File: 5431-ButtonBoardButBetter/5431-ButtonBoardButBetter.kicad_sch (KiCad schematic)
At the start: 17 parts, among them SW1 SW_DIP_x01, SW10 SW_DIP_x01, SW11 SW_DIP_x01, SW12 SW_DIP_x01, SW13 SW_DIP_x01, SW14 SW_DIP_x01, SW15 SW_DIP_x01, SW16 SW_DIP_x01, SW2 SW_DIP_x01, SW3 SW_DIP_x01, SW4 SW_DIP_x01, SW5 SW_DIP_x01, SW6 SW_DIP_x01, SW7 SW_DIP_x01, SW8 SW_DIP_x01, SW9 SW_DIP_x01, U1 Pico

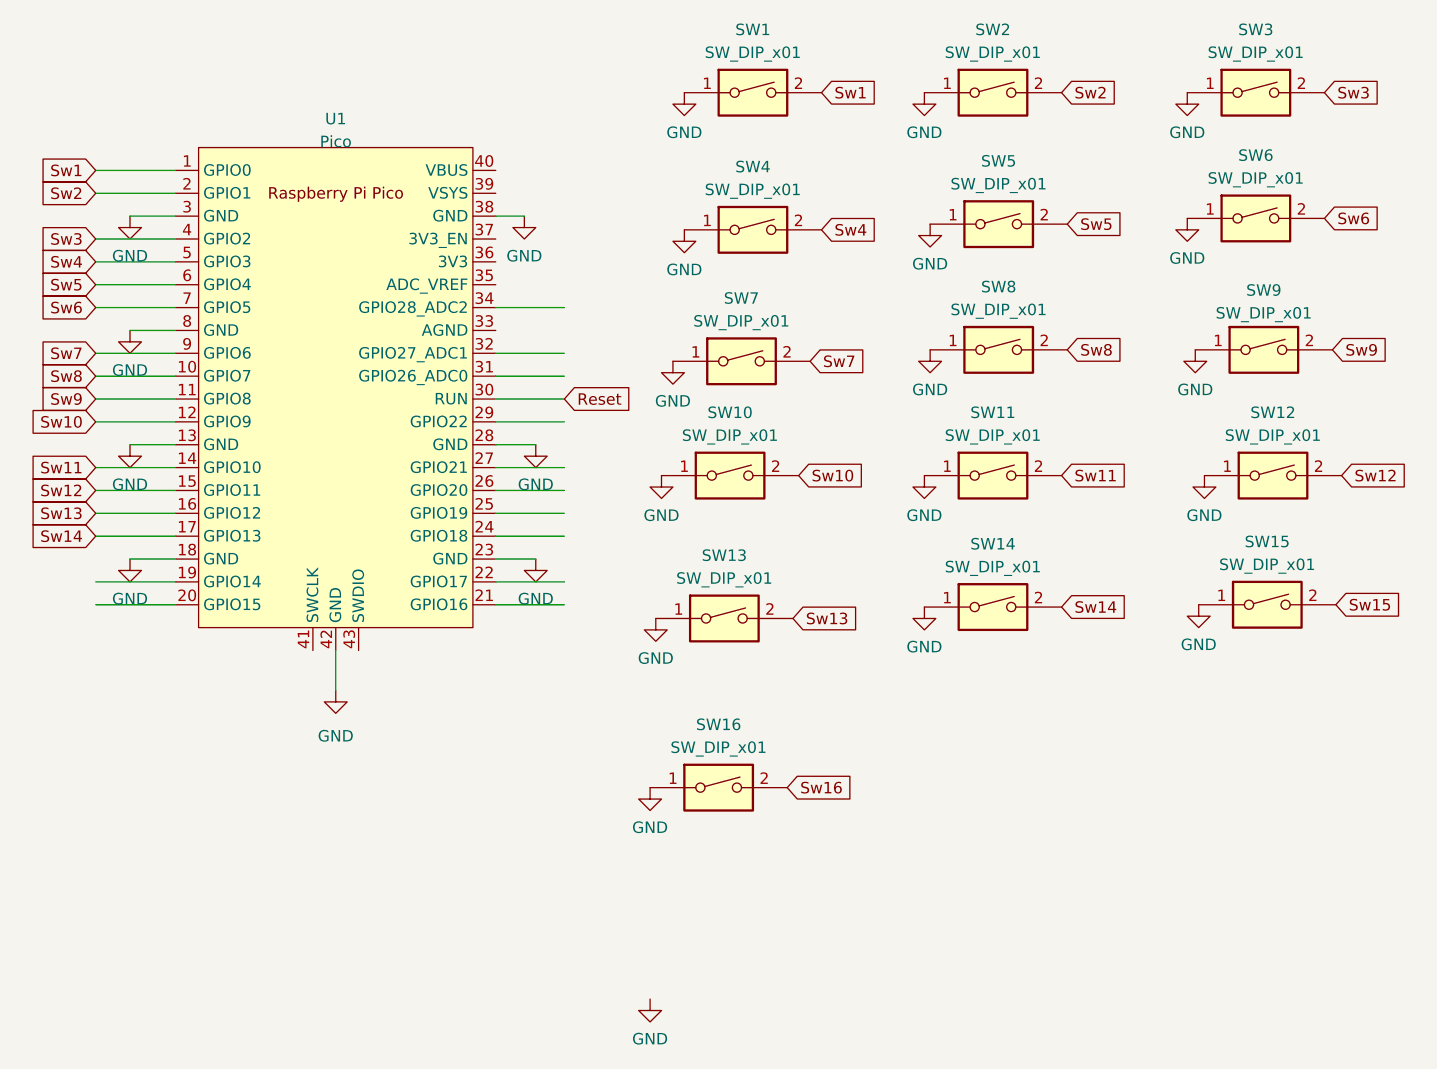
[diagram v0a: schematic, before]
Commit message: finished footprints
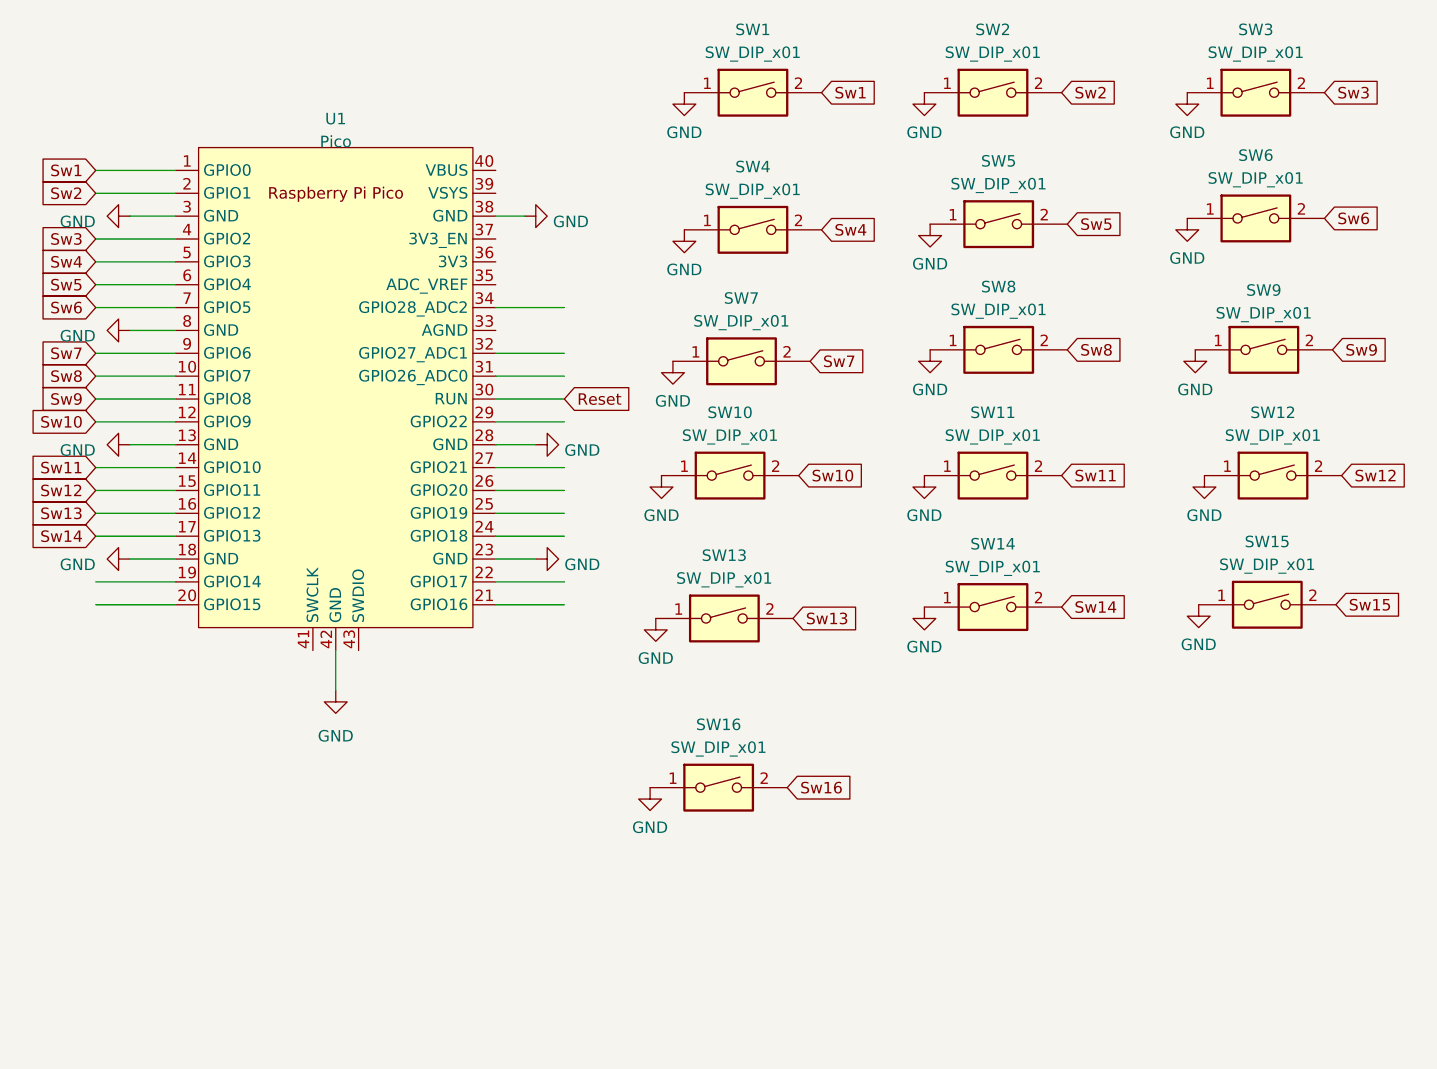
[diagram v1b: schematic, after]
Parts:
- SW1, SW10, SW11, SW12, SW13, SW14, SW15, SW16, SW2, SW3, SW5, SW6, SW7, SW8, SW9: footprint (none) -> Button_Switch_Keyboard:SW_Cherry_MX_1.00u_PCB
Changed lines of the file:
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@@
       (effects (font (size 1.27 1.27)))
     )
-    (property "Footprint" "" (at 204.47 115.189 0)
+    (property "Footprint" "Button_Switch_Keyboard:SW_Cherry_MX_1.00u_PCB" (at 204.47 115.189 0)
       (effects (font (size 1.27 1.27)) hide)
     )
@@
     )
   )
-  (symbol (lib_id "power:GND") (at 182.245 70.485 0) (unit 1)
-    (in_bom yes) (on_board yes) (dnp no) (fields_autoplaced)
-    (property "Reference" "#PWR01" (at 182.245 76.835 0)
-      (effects (font (size 1.27 1.27)) hide)
-    )
-    (property "Value" "GND" (at 182.245 74.93 0)
-      (effects (font (size 1.27 1.27)))
+  (symbol (lib_id "power:GND") (at 182.245 70.485 90) (unit 1)
+    (in_bom yes) (on_board yes) (dnp no) (fields_autoplaced)
+    (property "Reference" "#PWR01" (at 188.595 70.485 0)
+      (effects (font (size 1.27 1.27)) hide)
+    )
+    (property "Value" "GND" (at 185.42 71.12 90)
+      (effects (font (size 1.27 1.27)) (justify right))
     )
     (property "Footprint" "" (at 182.245 70.485 0)
@@
     )
   )
-  (symbol (lib_id "power:GND") (at 138.43 95.885 0) (unit 1)
-    (in_bom yes) (on_board yes) (dnp no) (fields_autoplaced)
-    (property "Reference" "#PWR024" (at 138.43 102.235 0)
-      (effects (font (size 1.27 1.27)) hide)
-    )
-    (property "Value" "GND" (at 138.43 100.33 0)
-      (effects (font (size 1.27 1.27)))
+  (symbol (lib_id "power:GND") (at 138.43 95.885 270) (unit 1)
+    (in_bom yes) (on_board yes) (dnp no) (fields_autoplaced)
+    (property "Reference" "#PWR024" (at 132.08 95.885 0)
+      (effects (font (size 1.27 1.27)) hide)
+    )
+    (property "Value" "GND" (at 134.62 96.52 90)
+      (effects (font (size 1.27 1.27)) (justify right))
     )
     (property "Footprint" "" (at 138.43 95.885 0)
@@
       (effects (font (size 1.27 1.27)))
     )
-    (property "Footprint" "" (at 234.315 113.919 0)
+    (property "Footprint" "Button_Switch_Keyboard:SW_Cherry_MX_1.00u_PCB" (at 234.315 113.919 0)
       (effects (font (size 1.27 1.27)) hide)
     )
@@
       (effects (font (size 1.27 1.27)))
     )
-    (property "Footprint" "" (at 234.95 85.344 0)
+    (property "Footprint" "Button_Switch_Keyboard:SW_Cherry_MX_1.00u_PCB" (at 234.95 85.344 0)
       (effects (font (size 1.27 1.27)) hide)
     )
@@
       (effects (font (size 1.27 1.27)))
     )
-    (property "Footprint" "" (at 234.95 71.374 0)
+    (property "Footprint" "Button_Switch_Keyboard:SW_Cherry_MX_1.00u_PCB" (at 234.95 71.374 0)
       (effects (font (size 1.27 1.27)) hide)
     )
@@
       (effects (font (size 1.27 1.27)))
     )
-    (property "Footprint" "" (at 234.315 99.314 0)
+    (property "Footprint" "Button_Switch_Keyboard:SW_Cherry_MX_1.00u_PCB" (at 234.315 99.314 0)
       (effects (font (size 1.27 1.27)) hide)
     )
@@
       (effects (font (size 1.27 1.27)))
     )
-    (property "Footprint" "" (at 203.835 133.985 0)
+    (property "Footprint" "Button_Switch_Keyboard:SW_Cherry_MX_1.00u_PCB" (at 203.835 133.985 0)
       (effects (font (size 1.27 1.27)) hide)
     )
@@
       (effects (font (size 1.27 1.27)))
     )
-    (property "Footprint" "" (at 264.795 113.665 0)
+    (property "Footprint" "Button_Switch_Keyboard:SW_Cherry_MX_1.00u_PCB" (at 264.795 113.665 0)
       (effects (font (size 1.27 1.27)) hide)
     )
@@
     )
   )
-  (symbol (lib_id "power:GND") (at 138.43 70.485 0) (unit 1)
-    (in_bom yes) (on_board yes) (dnp no) (fields_autoplaced)
-    (property "Reference" "#PWR03" (at 138.43 76.835 0)
-      (effects (font (size 1.27 1.27)) hide)
-    )
-    (property "Value" "GND" (at 138.43 74.93 0)
-      (effects (font (size 1.27 1.27)))
+  (symbol (lib_id "power:GND") (at 138.43 70.485 270) (unit 1)
+    (in_bom yes) (on_board yes) (dnp no) (fields_autoplaced)
+    (property "Reference" "#PWR03" (at 132.08 70.485 0)
+      (effects (font (size 1.27 1.27)) hide)
+    )
+    (property "Value" "GND" (at 134.62 71.12 90)
+      (effects (font (size 1.27 1.27)) (justify right))
     )
     (property "Footprint" "" (at 138.43 70.485 0)
@@
       (effects (font (size 1.27 1.27)))
     )
-    (property "Footprint" "" (at 206.375 86.614 0)
+    (property "Footprint" "Button_Switch_Keyboard:SW_Cherry_MX_1.00u_PCB" (at 206.375 86.614 0)
       (effects (font (size 1.27 1.27)) hide)
     )
@@
       (effects (font (size 1.27 1.27)))
     )
-    (property "Footprint" "" (at 263.525 70.739 0)
+    (property "Footprint" "Button_Switch_Keyboard:SW_Cherry_MX_1.00u_PCB" (at 263.525 70.739 0)
       (effects (font (size 1.27 1.27)) hide)
     )
@@
       (effects (font (size 1.27 1.27)))
     )
-    (property "Footprint" "" (at 207.645 56.769 0)
+    (property "Footprint" "Button_Switch_Keyboard:SW_Cherry_MX_1.00u_PCB" (at 207.645 56.769 0)
       (effects (font (size 1.27 1.27)) hide)
     )
@@
       (effects (font (size 1.27 1.27)))
     )
-    (property "Footprint" "" (at 263.525 56.769 0)
+    (property "Footprint" "Button_Switch_Keyboard:SW_Cherry_MX_1.00u_PCB" (at 263.525 56.769 0)
       (effects (font (size 1.27 1.27)) hide)
     )
@@
       (effects (font (size 1.27 1.27)))
     )
-    (property "Footprint" "" (at 264.414 85.344 0)
+    (property "Footprint" "Button_Switch_Keyboard:SW_Cherry_MX_1.00u_PCB" (at 264.414 85.344 0)
       (effects (font (size 1.27 1.27)) hide)
     )
@@
     )
   )
-  (symbol (lib_id "power:GND") (at 183.515 95.885 0) (unit 1)
-    (in_bom yes) (on_board yes) (dnp no) (fields_autoplaced)
-    (property "Reference" "#PWR025" (at 183.515 102.235 0)
-      (effects (font (size 1.27 1.27)) hide)
-    )
-    (property "Value" "GND" (at 183.515 100.33 0)
-      (effects (font (size 1.27 1.27)))
+  (symbol (lib_id "power:GND") (at 183.515 95.885 90) (unit 1)
+    (in_bom yes) (on_board yes) (dnp no) (fields_autoplaced)
+    (property "Reference" "#PWR025" (at 189.865 95.885 0)
+      (effects (font (size 1.27 1.27)) hide)
+    )
+    (property "Value" "GND" (at 186.69 96.52 90)
+      (effects (font (size 1.27 1.27)) (justify right))
     )
     (property "Footprint" "" (at 183.515 95.885 0)
@@
     )
   )
-  (symbol (lib_id "power:GND") (at 183.515 108.585 0) (unit 1)
-    (in_bom yes) (on_board yes) (dnp no) (fields_autoplaced)
-    (property "Reference" "#PWR026" (at 183.515 114.935 0)
-      (effects (font (size 1.27 1.27)) hide)
-    )
-    (property "Value" "GND" (at 183.515 113.03 0)
-      (effects (font (size 1.27 1.27)))
+  (symbol (lib_id "power:GND") (at 183.515 108.585 90) (unit 1)
+    (in_bom yes) (on_board yes) (dnp no) (fields_autoplaced)
+    (property "Reference" "#PWR026" (at 189.865 108.585 0)
+      (effects (font (size 1.27 1.27)) hide)
+    )
+    (property "Value" "GND" (at 186.69 109.22 90)
+      (effects (font (size 1.27 1.27)) (justify right))
     )
     (property "Footprint" "" (at 183.515 108.585 0)
@@
     )
   )
-  (symbol (lib_id "power:GND") (at 196.215 157.48 0) (unit 1)
-    (in_bom yes) (on_board yes) (dnp no) (fields_autoplaced)
-    (property "Reference" "#PWR030" (at 196.215 163.83 0)
-      (effects (font (size 1.27 1.27)) hide)
-    )
-    (property "Value" "GND" (at 196.215 161.925 0)
-      (effects (font (size 1.27 1.27)))
-    )
-    (property "Footprint" "" (at 196.215 157.48 0)
-      (effects (font (size 1.27 1.27)) hide)
-    )
-    (property "Datasheet" "" (at 196.215 157.48 0)
-      (effects (font (size 1.27 1.27)) hide)
-    )
-    (pin "1")
-    (instances
-      (project "5431-ButtonBoardButBetter"
-        (path "/85ad268b-acfd-4dd1-a78b-2229ab217983"
-          (reference "#PWR030") (unit 1)
-        )
-      )
-    )
-  )
   (symbol (lib_id "power:GND") (at 255.905 70.739 0) (unit 1)
     (in_bom yes) (on_board yes) (dnp no) (fields_autoplaced)
@@
     )
   )
-  (symbol (lib_id "power:GND") (at 138.43 108.585 0) (unit 1)
-    (in_bom yes) (on_board yes) (dnp no) (fields_autoplaced)
-    (property "Reference" "#PWR027" (at 138.43 114.935 0)
-      (effects (font (size 1.27 1.27)) hide)
-    )
-    (property "Value" "GND" (at 138.43 113.03 0)
-      (effects (font (size 1.27 1.27)))
+  (symbol (lib_id "power:GND") (at 138.43 108.585 270) (unit 1)
+    (in_bom yes) (on_board yes) (dnp no) (fields_autoplaced)
+    (property "Reference" "#PWR027" (at 132.08 108.585 0)
+      (effects (font (size 1.27 1.27)) hide)
+    )
+    (property "Value" "GND" (at 134.62 109.22 90)
+      (effects (font (size 1.27 1.27)) (justify right))
     )
     (property "Footprint" "" (at 138.43 108.585 0)
@@
       (effects (font (size 1.27 1.27)))
     )
-    (property "Footprint" "" (at 265.43 99.314 0)
+    (property "Footprint" "Button_Switch_Keyboard:SW_Cherry_MX_1.00u_PCB" (at 265.43 99.314 0)
       (effects (font (size 1.27 1.27)) hide)
     )
@@
       (effects (font (size 1.27 1.27)))
     )
-    (property "Footprint" "" (at 234.315 56.769 0)
+    (property "Footprint" "Button_Switch_Keyboard:SW_Cherry_MX_1.00u_PCB" (at 234.315 56.769 0)
       (effects (font (size 1.27 1.27)) hide)
     )
@@
       (effects (font (size 1.27 1.27)))
     )
-    (property "Footprint" "" (at 205.105 99.314 0)
+    (property "Footprint" "Button_Switch_Keyboard:SW_Cherry_MX_1.00u_PCB" (at 205.105 99.314 0)
       (effects (font (size 1.27 1.27)) hide)
     )
@@
     )
   )
-  (symbol (lib_id "power:GND") (at 138.43 83.185 0) (unit 1)
-    (in_bom yes) (on_board yes) (dnp no) (fields_autoplaced)
-    (property "Reference" "#PWR023" (at 138.43 89.535 0)
-      (effects (font (size 1.27 1.27)) hide)
-    )
-    (property "Value" "GND" (at 138.43 87.63 0)
-      (effects (font (size 1.27 1.27)))
+  (symbol (lib_id "power:GND") (at 138.43 83.185 270) (mirror x) (unit 1)
+    (in_bom yes) (on_board yes) (dnp no)
+    (property "Reference" "#PWR023" (at 132.08 83.185 0)
+      (effects (font (size 1.27 1.27)) hide)
+    )
+    (property "Value" "GND" (at 134.62 83.82 90)
+      (effects (font (size 1.27 1.27)) (justify right))
     )
     (property "Footprint" "" (at 138.43 83.185 0)
